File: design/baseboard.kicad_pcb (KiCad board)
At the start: 4 copper layers, 80 x 100 mm, 243 parts, among them J1 Conn_01x02_Male, J10 Conn_01x03_Male, J11 HDMI_A, J12 USB2.0_2Conn, J2 3-1734592-0, J3 Jack-DC, J4 Conn_01x04_Male, J5 NANO-nvidia_nano, J6 Conn_02x20_Odd_Even, J7 USB_B_Micro, J8 USB_B_Micro, J9 USB2.0_2Conn, Q1 2N7002, Q10 DMN26D0UFB4, Q11 DMN26D0UFB4, Q12 DMN26D0UFB4, Q13 DMN26D0UFB4, Q14 DMN26D0UFB4, Q2 2N7002, Q3 DMN26D0UFB4, Q4 DMN26D0UFB4, Q5 2N7002, Q6 DMN26D0UFB4, Q7 DMN26D0UFB4, Q8 MMBT3904, Q9 DMN26D0UFB4, U1 74LVC1G126, U10 MT9700, U15 TXB0102DCUR, U16 CH340G, U18 AT24CS01-SSHM-T, U2 74LVC1G07GW, U22 AP2281-3WG-7, U23 USB2514B-AEZG, U24 MC74VHC1G01DFT1G, U3 MC74VHC1G01DFT1G, U4 74LVC1G126, U5 TXS0108EPW, U6 TXS0108EPW, U7 TLV62569DDC, U8 TLV70018DCKT, U9 TXS0108EPW, Y1 X322524MMB4SI, Y2 X322512MSB4SI

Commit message: rename baseboard
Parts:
- J6: moved to B.Cu
- moved C39 8.11 mm to (2.90, 85.3), turned to 90 degrees
- moved C36 7.24 mm to (25.2, 90.5)
- moved J6 2.45 mm to (4.95, 88.0), turned to 270 degrees
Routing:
- net SLEEP_WAKE*: track 139.5 -> 107.6 mm, vias 5 -> 4
- net UART1_RTS_LS: track 41.7 -> 55.4 mm
- net I2S0_LRCK_LS: track 41.8 -> 53.6 mm, vias 2 -> 1
- net GPIO09_LS: track 60.4 -> 71.5 mm, vias 3 -> 2
- net SPI1_MISO_LS: track 85.1 -> 74.4 mm
- net I2C1_SCL: track 139.3 -> 131.0 mm, vias 3 -> 4
- net +3V3: track 50.9 -> 43.7 mm, vias 29 -> 34
- net GPIO12_LS: track 61.6 -> 68.5 mm
- net SPI1_CS1_LS: track 84.3 -> 78.0 mm, vias 1 -> 2
- net GPIO13_LS: track 53.8 -> 59.5 mm, vias 2 -> 1
- net UART1_RXD_LS: track 49.3 -> 44.0 mm, vias 2 -> 1
- net SPI0_MOSI_LS: track 55.4 -> 60.6 mm, vias 1 -> 2
- net 3V3_PGOOD: track 60.6 -> 65.5 mm
- net I2C0_SCL: track 97.9 -> 93.2 mm
- net +5V: track 107.2 -> 102.7 mm
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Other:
- board text added: "HDMI"
- board text added: "USB 2.0"
- board text removed: "HDMI input"
- board text removed: "USB 2.0 Connection"

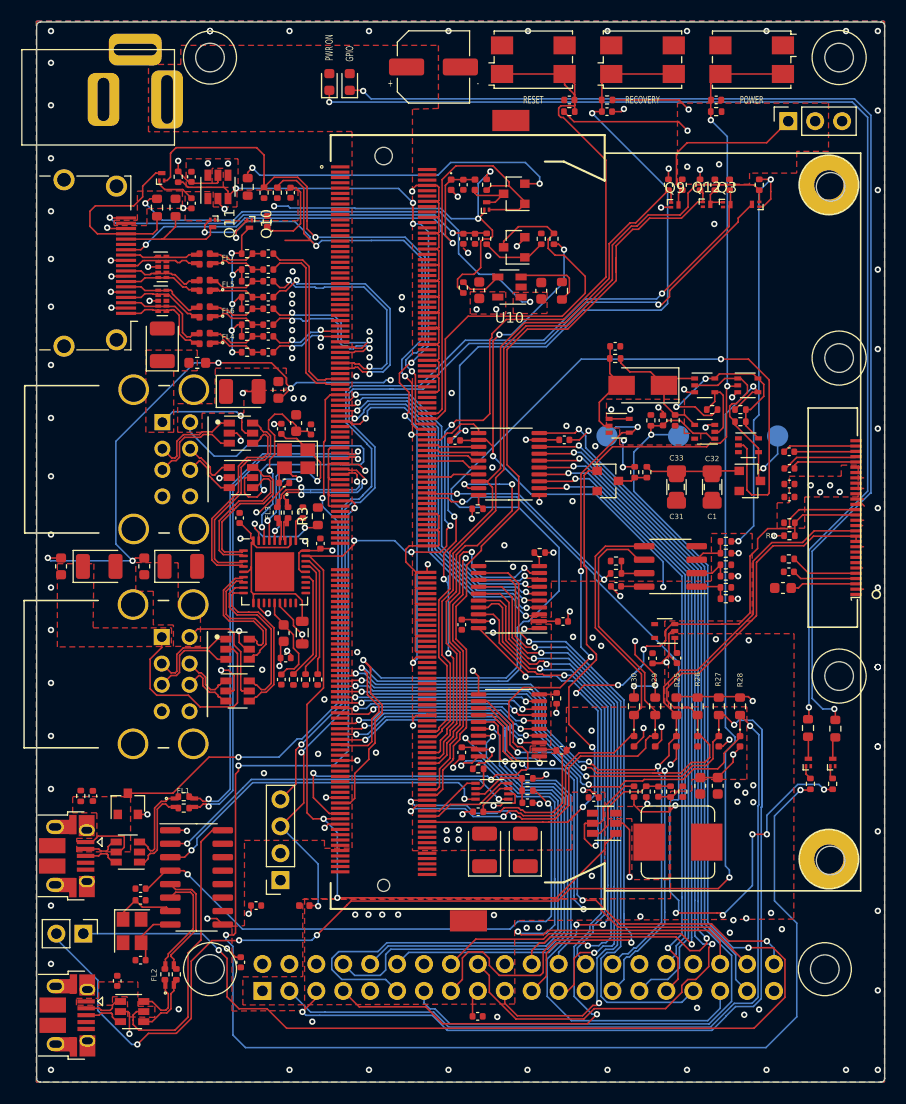
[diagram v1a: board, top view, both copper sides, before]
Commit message: rename & move files for cohesion
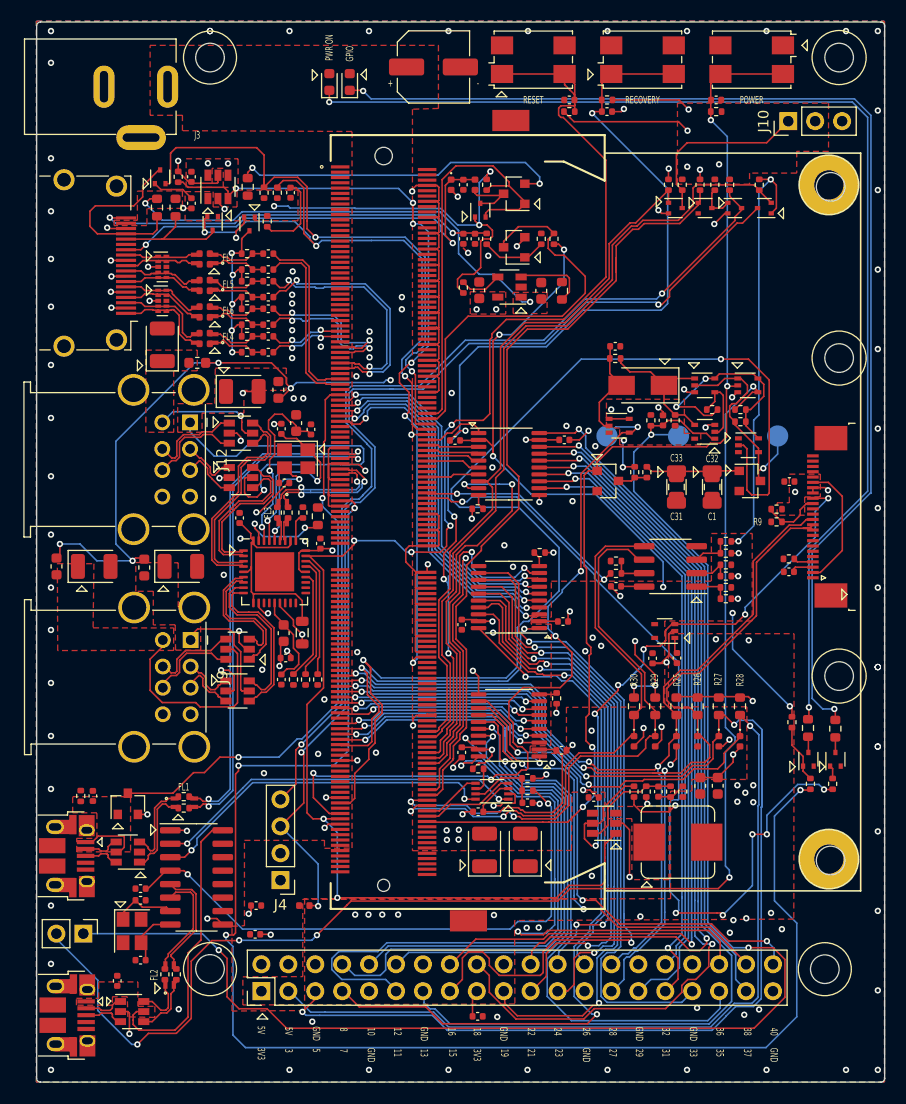
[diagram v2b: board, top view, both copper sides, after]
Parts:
- removed C5, C6, C7: 1uF, Capacitor_SMD:C_0402_1005Metric
- removed C9: 2.2uF, Capacitor_SMD:C_0603_1608Metric
- added R89: 10k, Resistor_SMD:R_0402_1005Metric, F.Cu at (54.9, 62.7)
- J10: footprint Connector_PinSocket_2.54mm:PinSocket_1x03_P2.54mm_Vertical -> Connector_PinHeader_2.54mm:PinHeader_1x03_P2.54mm_Vertical
- J12, J9: footprint Libraries:Molex-67298-3090-0 -> Connector_USB:USB_A_Wuerth_61400826021_Horizontal_Stacked
- J2: value 3-1734592-0 -> Conn_01x24_Female; footprint Libraries:3-1734592-0 -> Connector_FFC-FPC:TE_2-1734839-4_1x24-1MP_P0.5mm_Horizontal
- J3: footprint Downloads:DC_JACK_DC-005-5A-2.0_clearance -> Custom Footprints:NINIGI_DC-005
- J4: footprint Connector_PinSocket_2.54mm:PinSocket_1x04_P2.54mm_Vertical -> Connector_PinHeader_2.54mm:PinHeader_1x04_P2.54mm_Vertical
- J6: footprint Connector_PinSocket_2.54mm:PinSocket_2x20_P2.54mm_Vertical -> Connector_PinHeader_2.54mm:PinHeader_2x20_P2.54mm_Vertical; moved to F.Cu
- Q10, Q11, Q12, Q13, Q14, Q3, Q4, Q6, Q7, Q9: value DMN26D0UFB4 -> DMN26D0UT-7; footprint Package_DFN_QFN:Diodes_DFN1006-3 -> Package_TO_SOT_SMD:SOT-523
- R91: value 120k -> 11k
- moved J3 12.5 mm to (-6.50, 2.75)
- moved TH4 8.28 mm to (-14.5, 48.0)
- moved C66 8.17 mm to (-10.9, 48.0)
- moved TH3 7.85 mm to (-6.20, 48.1)
- moved J12 7.77 mm to (-1.88, 34.4)
- moved J9 7.76 mm to (-1.83, 55.0)
- moved C68 7.70 mm to (-2.75, 48.0)
- moved J2 7.68 mm to (58.2, 43.3)
- moved C39 2.97 mm to (4.26, 82.7), turned to 0 degrees
- moved R9 1.79 mm to (53.5, 43.8)
- moved R10 1.77 mm to (53.5, 42.6), turned to 0 degrees
- moved C4 1.45 mm to (54.7, 40.0)
- moved Q4 0.90 mm to (52.3, 14.2)
- moved Q3 0.82 mm to (49.5, 14.2)
- moved Q14 0.72 mm to (25.5, 14.4)
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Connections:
- C66 pad 1: /USB2.0 Type A Hub/USB_DSP1_VBUS -> /USB2.0 Type A Hub/USB_DSP3_VBUS
- C67 pad 1: /USB2.0 Type A Hub/USB_DSP2_VBUS -> /USB2.0 Type A Hub/USB_DSP4_VBUS
- C68 pad 1: /USB2.0 Type A Hub/USB_DSP3_VBUS -> /USB2.0 Type A Hub/USB_DSP1_VBUS
- C69 pad 1: /USB2.0 Type A Hub/USB_DSP4_VBUS -> /USB2.0 Type A Hub/USB_DSP2_VBUS
- J12 pad 1: /USB2.0 Type A Hub/USB_DSP4_VBUS -> /USB2.0 Type A Hub/USB_DSP2_VBUS
- J12 pad 2: /USB2.0 Type A Hub/USB_DSP4_DN -> /USB2.0 Type A Hub/USB_DSP2_DN
- J12 pad 3: /USB2.0 Type A Hub/USB_DSP4_DP -> /USB2.0 Type A Hub/USB_DSP2_DP
- J12 pad 5: /USB2.0 Type A Hub/USB_DSP2_VBUS -> /USB2.0 Type A Hub/USB_DSP4_VBUS
- J12 pad 6: /USB2.0 Type A Hub/USB_DSP2_DN -> /USB2.0 Type A Hub/USB_DSP4_DN
- J12 pad 7: /USB2.0 Type A Hub/USB_DSP2_DP -> /USB2.0 Type A Hub/USB_DSP4_DP
- J2 pad 1: GND -> (no net)
- J2 pad 10: GND -> I2C0_SDA
- J2 pad 12: I2C0_SDA -> I2C0_SCL
- J2 pad 13: I2C0_SCL -> GND
- J2 pad 15: GND -> /OLED Display/DATA_CMD
- J2 pad 16: /OLED Display/DATA_CMD -> 3V3_PGOOD
- J2 pad 17: 3V3_PGOOD -> GND
- J2 pad 19: GND -> +3V3
- J2 pad 2: GND -> +3V3
- J2 pad 21: GND -> (no net)
- J2 pad 22: +3V3 -> GND
- J2 pad 3: /OLED Display/OLED_OEL_PWR -> /OLED Display/OLED_COM_HI
- J2 pad 4: /OLED Display/OLED_COM_HI -> /OLED Display/IREF
- J2 pad 5: /OLED Display/IREF -> GND
- J3 pad 3: (no net) -> GND
- J9 pad 1: /USB2.0 Type A Hub/USB_DSP3_VBUS -> /USB2.0 Type A Hub/USB_DSP1_VBUS
- J9 pad 2: /USB2.0 Type A Hub/USB_DSP3_DN -> /USB2.0 Type A Hub/USB_DSP1_DN
- J9 pad 3: /USB2.0 Type A Hub/USB_DSP3_DP -> /USB2.0 Type A Hub/USB_DSP1_DP
- J9 pad 5: /USB2.0 Type A Hub/USB_DSP1_VBUS -> /USB2.0 Type A Hub/USB_DSP3_VBUS
- J9 pad 6: /USB2.0 Type A Hub/USB_DSP1_DN -> /USB2.0 Type A Hub/USB_DSP3_DN
- J9 pad 7: /USB2.0 Type A Hub/USB_DSP1_DP -> /USB2.0 Type A Hub/USB_DSP3_DP
- TH1 pad 1: /USB2.0 Type A Hub/USB_DSP4_VBUS -> /USB2.0 Type A Hub/USB_DSP2_VBUS
- TH2 pad 1: /USB2.0 Type A Hub/USB_DSP2_VBUS -> /USB2.0 Type A Hub/USB_DSP4_VBUS
- TH3 pad 1: /USB2.0 Type A Hub/USB_DSP3_VBUS -> /USB2.0 Type A Hub/USB_DSP1_VBUS
- TH4 pad 1: /USB2.0 Type A Hub/USB_DSP1_VBUS -> /USB2.0 Type A Hub/USB_DSP3_VBUS
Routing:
- net +1V8: track 123.1 -> 135.6 mm, vias 12 -> 14
- net +3V3: track 43.7 -> 55.8 mm, vias 34 -> 35
- net /OLED Display/INV_CAP_N: track 7.23 -> 0.00 mm
- net /OLED Display/BST_CAP_N: track 7.02 -> 0.00 mm
- net 3V3_PGOOD: track 65.5 -> 58.8 mm, vias 4 -> 6
- net /OLED Display/OLED_OEL_PWR: track 6.28 -> 0.00 mm
- net /OLED Display/INV_CAP_P: track 6.24 -> 0.00 mm
- net /OLED Display/BST_CAP_P: track 5.85 -> 0.00 mm
- net /OLED Display/IREF: track 6.39 -> 1.87 mm
- net Net-(Q7-Pad1): track 1.33 -> 5.52 mm
- net /OLED Display/OLED_COM_HI: track 6.12 -> 2.15 mm
- net GND: track 214.5 -> 210.5 mm, vias 170 -> 171
- net I2C0_SCL: track 93.2 -> 89.6 mm
- net I2C0_SDA: track 101.8 -> 99.0 mm
- net HDMI_DDC_SCL_POL: track 54.3 -> 52.1 mm
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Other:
- board text added: "10"
- board text added: "11"
- board text added: "12"
- board text added: "13"
- board text added: "15"
- board text added: "16"
- board text added: "18"
- board text added: "19"
- board text added: "21"
- board text added: "22"
- board text added: "23"
- board text added: "24"
- board text added: "26"
- board text added: "27"
- board text added: "28"
- board text added: "29"
- board text added: "3"
- board text added: "31"
- board text added: "32"
- board text added: "33"
- board text added: "35"
- board text added: "36"
- board text added: "37"
- board text added: "38"
- board text added: "3V3"
- board text added: "40"
- board text added: "5"
- board text added: "7"
- board text added: "8"
